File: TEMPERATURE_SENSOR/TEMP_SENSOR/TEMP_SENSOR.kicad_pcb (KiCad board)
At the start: 2 copper layers, 25.9 x 33.1 mm, 10 parts, among them J1 Conn_01x04_Pin, U1 LM393

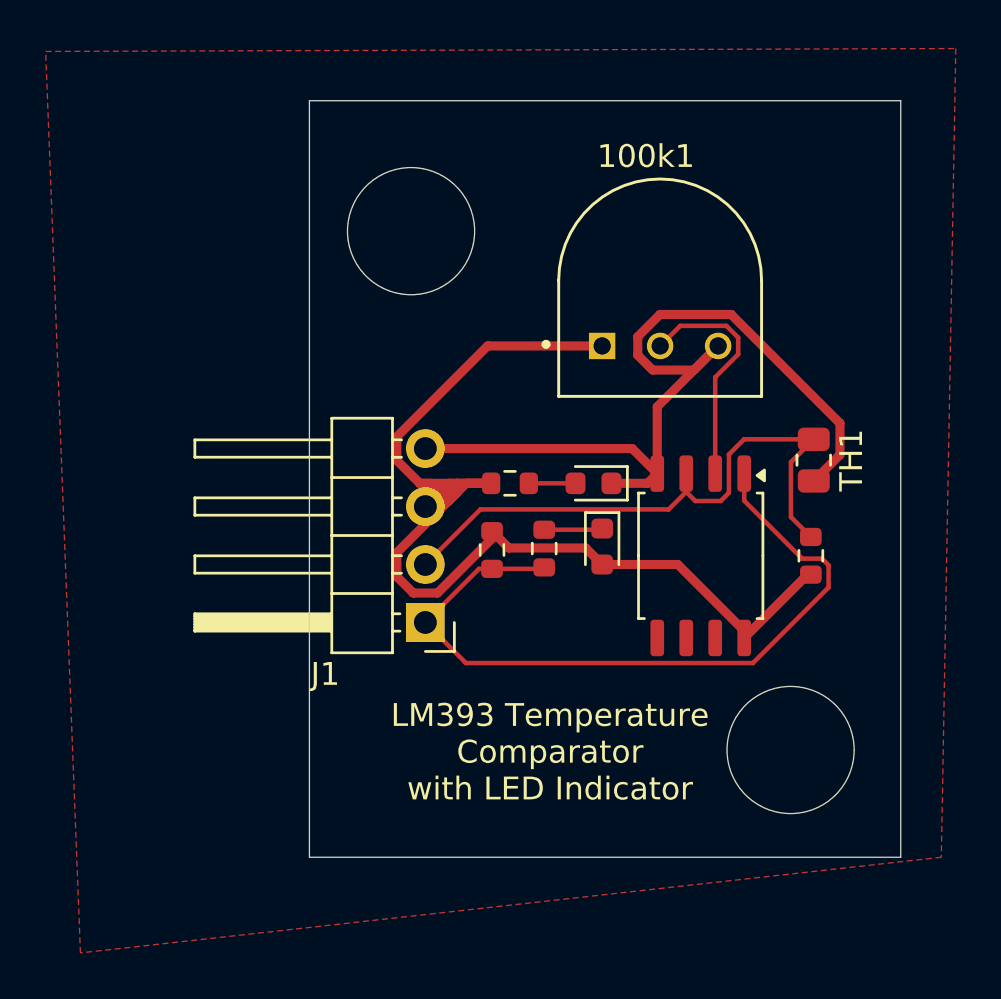
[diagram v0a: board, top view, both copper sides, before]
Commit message: temp sensor module refined and audio amplifier made
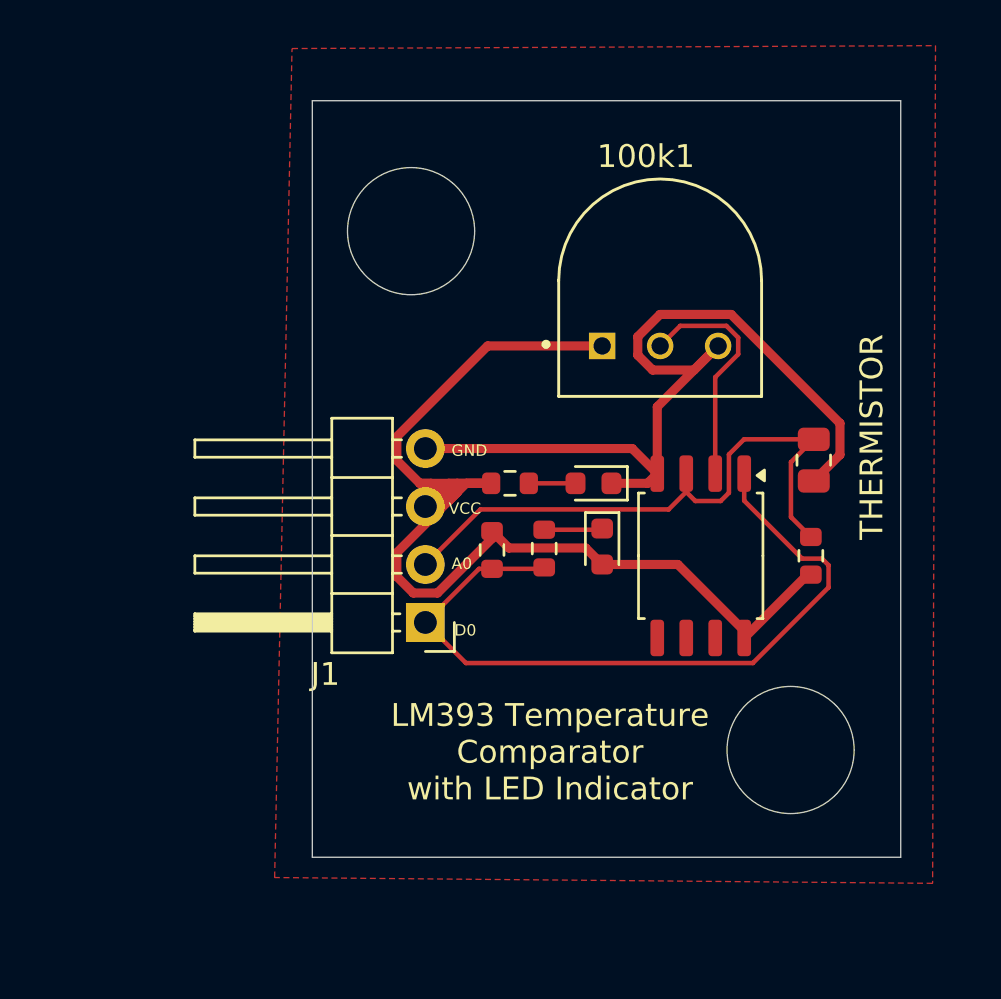
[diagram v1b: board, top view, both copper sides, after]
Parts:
- renumbered TH1 to THERMISTOR
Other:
- board size 25.9 x 33.1 mm -> 25.8 x 33.1 mm
- board text added: "A0"
- board text added: "D0"
- board text added: "GND"
- board text added: "VCC"
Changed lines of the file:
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@@
 		(tags "Through hole angled pin header THT 1x04 2.54mm single row")
 		(property "Reference" "J1"
-			(at 4.385 -2.27 360)
+			(at 4.385 -2.27 0)
 			(layer "F.SilkS")
 			(effects
@@
 		)
 		(property "Value" "Conn_01x04_Pin"
-			(at 4.385 9.89 360)
+			(at 4.385 9.89 0)
 			(layer "F.Fab")
 			(effects
@@
 		(descr "Resistor SMD 0805 (2012 Metric), square (rectangular) end terminal, IPC_7351 nominal, (Body size source: IPC-SM-782 page 72, https://www.pcb-3d.com/wordpress/wp-content/uploads/ipc-sm-782a_amendment_1_and_2.pdf), generated with kicad-footprint-generator")
 		(tags "resistor")
-		(property "Reference" "TH1"
-			(at 0 -1.65 90)
+		(property "Reference" "THERMISTOR"
+			(at -1.016 -2.54 90)
 			(layer "F.SilkS")
 			(effects
@@
 		(tags "LED")
 		(property "Reference" "D2"
-			(at 0 -1.43 360)
+			(at 0 -1.43 0)
 			(layer "F.SilkS")
 			(hide yes)
@@
 		)
 		(property "Value" "LED"
-			(at 0 1.43 360)
+			(at 0 1.43 0)
 			(layer "F.Fab")
 			(effects
@@
 		)
 		(fp_text user "${REFERENCE}"
-			(at 0 0 360)
+			(at 0 0 0)
 			(layer "F.Fab")
 			(effects
@@
 		(tags "resistor")
 		(property "Reference" "R3"
-			(at 0 -1.43 360)
+			(at 0 -1.43 0)
 			(layer "F.SilkS")
 			(hide yes)
@@
 		)
 		(property "Value" "1k"
-			(at 0 1.43 360)
+			(at 0 1.43 0)
 			(layer "F.Fab")
 			(effects
@@
 		)
 		(fp_text user "${REFERENCE}"
-			(at 0 0 360)
+			(at 0 0 0)
 			(layer "F.Fab")
 			(effects
@@
 	)
 	(gr_rect
-		(start 126.238 74.676)
+		(start 126.365 74.676)
 		(end 152.146 107.823)
 		(stroke
@@
 		(fill none)
 		(layer "Edge.Cuts")
+	)
+	(gr_text "GND"
+		(at 132.461 90.297 0)
+		(layer "F.SilkS")
+		(effects
+			(font
+				(size 0.5 0.5)
+				(thickness 0.075)
+			)
+			(justify left bottom)
+		)
+	)
+	(gr_text "A0\n"
+		(at 132.461 95.25 0)
+		(layer "F.SilkS")
+		(effects
+			(font
+				(size 0.5 0.5)
+				(thickness 0.1)
+			)
+			(justify left bottom)
+		)
+	)
+	(gr_text "D0\n"
+		(at 132.588 98.171 0)
+		(layer "F.SilkS")
+		(effects
+			(font
+				(size 0.5 0.5)
+				(thickness 0.1)
+			)
+			(justify left bottom)
+		)
+	)
+	(gr_text "VCC"
+		(at 132.334 92.837 0)
+		(layer "F.SilkS")
+		(effects
+			(font
+				(size 0.5 0.5)
+				(thickness 0.1)
+			)
+			(justify left bottom)
+		)
 	)
 	(gr_text "LM393 Temperature \nComparator \nwith LED Indicator"
@@
 		(min_thickness 0.25)
 		(filled_areas_thickness no)
-		(fill yes
+		(fill
 			(thermal_gap 0.5)
 			(thermal_bridge_width 0.5)
@@
 		(polygon
 			(pts
-				(xy 114.681 72.517) (xy 154.559 72.39) (xy 153.924 107.823) (xy 116.205 112.014)
-			)
-		)
+				(xy 125.476 72.39) (xy 153.67 72.263) (xy 153.543 108.966) (xy 124.714 108.712)
+			)
+		)
